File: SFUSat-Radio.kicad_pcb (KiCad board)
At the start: 4 copper layers, 95.9 x 90.2 mm, 283 parts, among them J1 PC104-8BIT, J10 TP_TH_150, J11 TP_TH_150, J12 SMA, J13 SMA, J14 SMA, J15 Conn_01x02, J16 SMA, J17 SMA, J18 SMA, J19 Conn_01x03, J2 PC104PTH, J20 Conn_01x03, J21 TP_TH_150, J22 TP_TH_150, J23 TP_TH_150, J24 TP_TH_150, J25 Conn_01x02, J3 PC104PTH, J4 PC104PTH, J400 SMA, J401 TP_TH_150, J402 TP_TH_150, J404 TP_TH_150, J405 TP_TH_150, J406 TP_TH_150, J5 PC104PTH, J500 SMA, J501 TP_TH_150, J502 TP_TH_150, J504 TP_TH_150, J505 TP_TH_150, J506 TP_TH_150, J6 SMA, J7 TP_TH_150, J8 TP_TH_150, J9 TP_TH_150, U1 SINGLE_0402, U10 TPS799, U100 CC1101-Q1, U101 0433BM15A0001, U11 SINGLE_0402, U110 CC1101-Q1, U111 0915BM15A0001E, U12 CONN_02X05_SHRD, U13 CONN_02X05_SHRD, U14 2N7002DW, U15 TPS62175DQCR, U16 TPS71750DSER, U17 74LVC1G14SE-7, U2 SKY13345-368LF, U3 CD4555BPWR, U4 LMS3635AQRNLRQ1, U400 SINGLE_0402, U401 LMV358, U402 RF6886, U420 2N7002DW, U5 MML09211H, U500 SINGLE_0402, U501 LMV358, U502 RF6886, U6 SINGLE_0402, U600 STLM75, U610 STLM75, U7 SKY13372-467LF, U8 SINGLE_0402, U9 TLV702, X100 NX3225GA, X110 NX3225GA

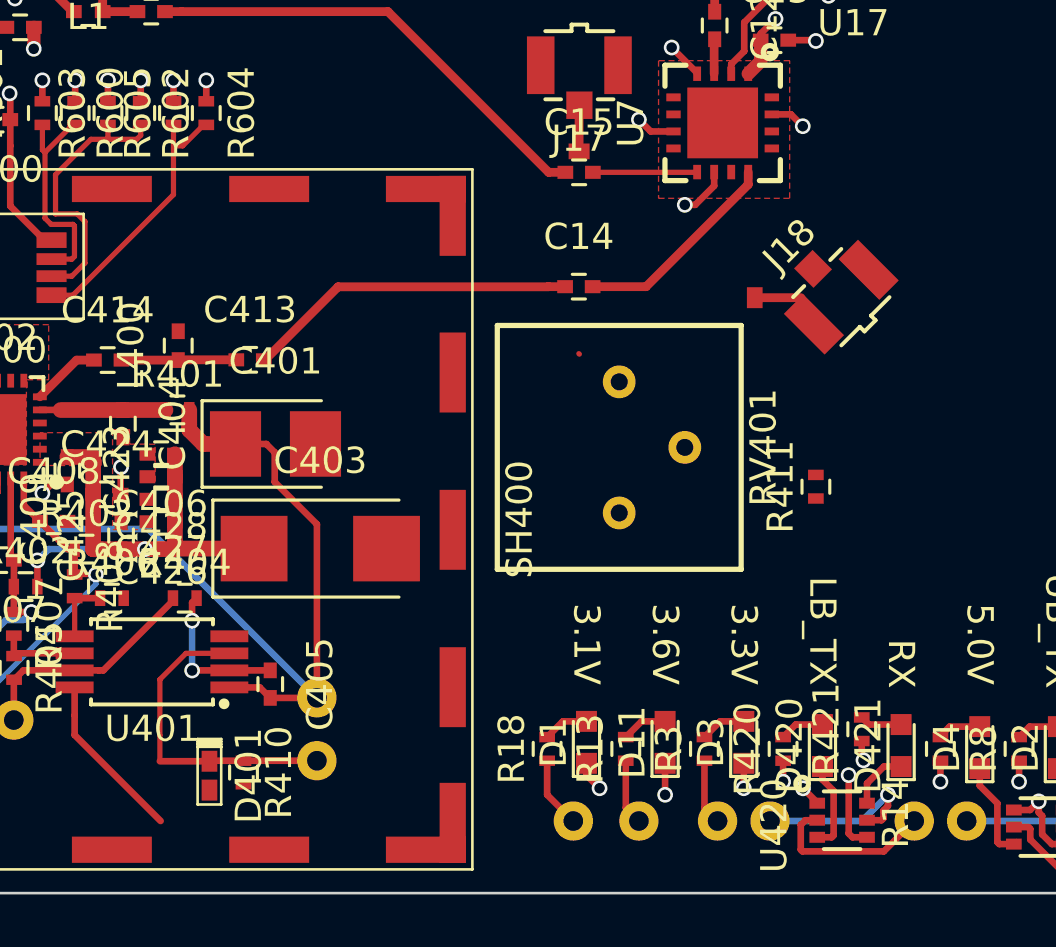
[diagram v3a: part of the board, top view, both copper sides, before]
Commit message: fixed LB cc1101 test point
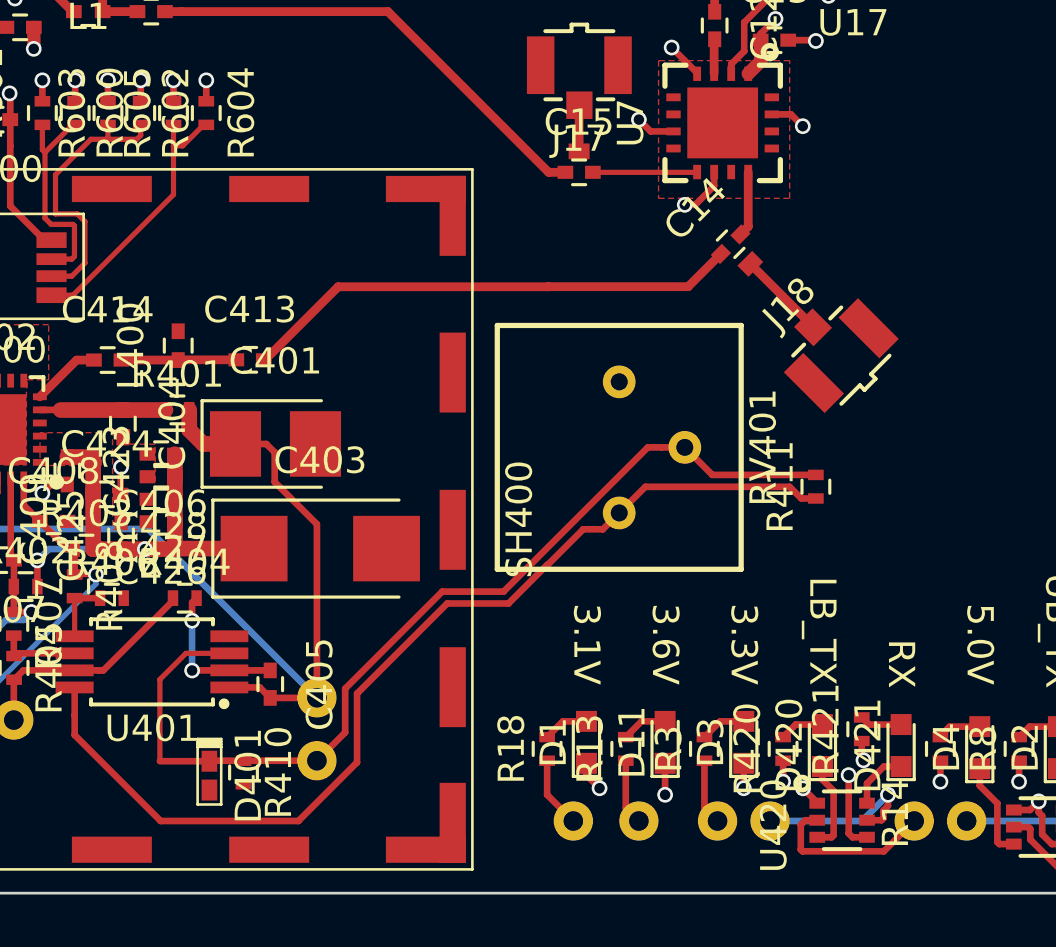
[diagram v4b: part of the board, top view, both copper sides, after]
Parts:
- moved C14 6.01 mm to (180.8, 123.8), turned to 45 degrees
- moved J18 2.23 mm to (185.0, 128.0)
- moved U8 1.30 mm to (181.5, 124.5), turned to 225 degrees
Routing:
- net /3V1: track 96.1 -> 128.1 mm
- net /PA_LB/GAIN: track 12.2 -> 37.6 mm
- net /LB_LP_TX: track 12.6 -> 19.1 mm
- net Net-(C14-Pad2): track 8.02 -> 2.50 mm
- net Net-(J18-Pad1): track 1.78 -> 3.41 mm

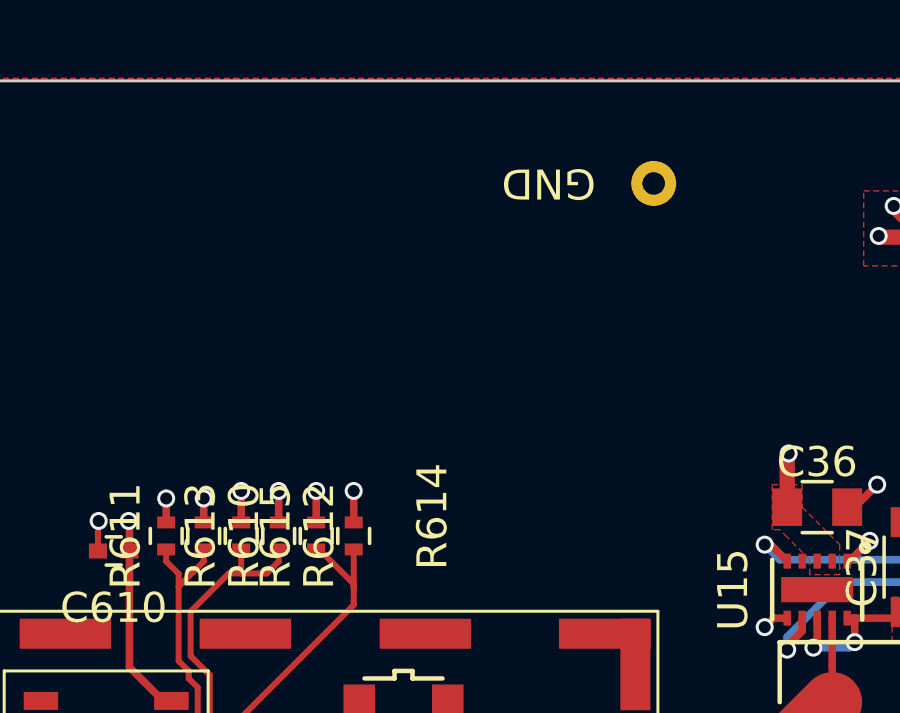
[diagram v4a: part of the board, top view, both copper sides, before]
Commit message: Added barrel jack for Vin; closes 46
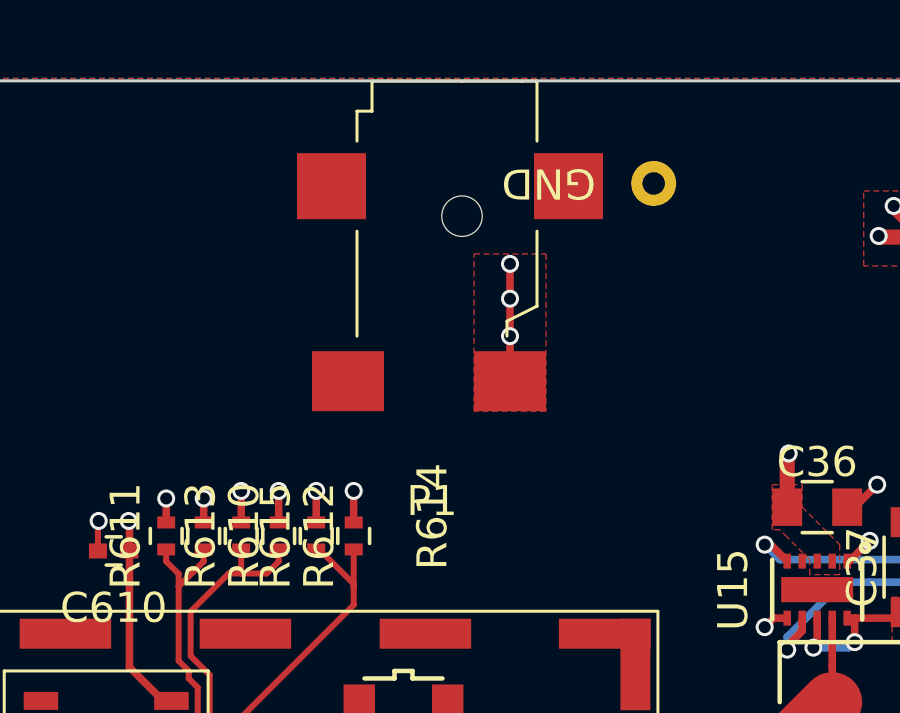
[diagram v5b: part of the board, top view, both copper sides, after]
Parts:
- added P1: 3pin-DC-power, SFUSat:PJ-028-SMT-TR-3pin-DC-jack, F.Cu at (146.4, 62.8)
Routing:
- net /VIN: track 12.4 -> 16.3 mm, vias 4 -> 7
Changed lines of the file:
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@@
-(kicad_pcb (version 4) (host pcbnew 4.0.7-e2-6376~58~ubuntu16.04.1)
+(kicad_pcb (version 4) (host pcbnew 4.0.5)
   (general
-    (links 728)
-    (no_connects 103)
+    (links 732)
+    (no_connects 78)
     (area 112.449999 58.279999 208.440001 148.550001)
     (thickness 1.6)
     (drawings 26)
-    (tracks 1228)
+    (tracks 1234)
     (zones 0)
-    (modules 283)
+    (modules 284)
     (nets 207)
   )
@@
     )
   )
+  (module SFUSat:PJ-028-SMT-TR-3pin-DC-jack (layer F.Cu)
+    (at 146.36 62.84 270)
+    (fp_text reference P1 (at 9.5 1 360) (layer F.SilkS)
+      (effects (font (size 1 1) (thickness 0.15)))
+    )
+    (fp_text value 3pin-DC-power (at 3.5 -6.5 270) (layer F.Fab)
+      (effects (font (size 1 1) (thickness 0.15)))
+    )
+    (fp_line (start 3.5 -1.5) (end 4 -1.5) (layer F.SilkS) (width 0.1))
+    (fp_line (start 3 -2.5) (end 3.5 -1.5) (layer F.SilkS) (width 0.1))
+    (fp_line (start 0.5 -2.5) (end 3 -2.5) (layer F.SilkS) (width 0.1))
+    (fp_line (start 0.5 3.5) (end 4 3.5) (layer F.SilkS) (width 0.1))
+    (fp_line (start -4.5 -2.5) (end -2.5 -2.5) (layer F.SilkS) (width 0.1))
+    (fp_line (start -4.5 -2) (end -4.5 -2.5) (layer F.SilkS) (width 0.1))
+    (fp_line (start -4.5 3) (end -4.5 0) (layer F.SilkS) (width 0.1))
+    (fp_line (start -3.5 3) (end -4.5 3) (layer F.SilkS) (width 0.1))
+    (fp_line (start -3.5 3.5) (end -3.5 3) (layer F.SilkS) (width 0.1))
+    (fp_line (start -2.5 3.5) (end -3.5 3.5) (layer F.SilkS) (width 0.1))
+    (fp_line (start -4.5 0) (end -4.5 -2) (layer F.SilkS) (width 0.1))
+    (pad 3 smd rect (at -1 -3.55 270) (size 2.2 2.3) (layers F.Cu F.Paste F.Mask)
+      (net 1 GND))
+    (pad "" np_thru_hole circle (at 0 0 270) (size 1.35 1.35) (drill 1.35) (layers *.Cu *.Mask))
+    (pad 3 smd rect (at -1 4.35 270) (size 2.2 2.3) (layers F.Cu F.Paste F.Mask)
+      (net 1 GND))
+    (pad 2 smd rect (at 5.5 3.8 270) (size 2 2.4) (layers F.Cu F.Paste F.Mask)
+      (net 1 GND))
+    (pad 1 smd rect (at 5.5 -1.6 270) (size 2 2.4) (layers F.Cu F.Paste F.Mask)
+      (net 183 /VIN))
+  )
   (gr_text GND (at 149.25 61.75 180) (layer F.SilkS)
     (effects (font (size 1 1) (thickness 0.15)))
@@
   (segment (start 182.42 96.13) (end 182.82 95.73) (width 0.2) (layer F.Cu) (net 170))
   (segment (start 182.82 95.73) (end 184.095 95.73) (width 0.2) (layer F.Cu) (net 170))
+  (segment (start 147.96 65.59) (end 147.96 64.43) (width 0.254) (layer F.Cu) (net 183))
+  (via (at 147.96 64.43) (size 0.6) (drill 0.4) (layers F.Cu B.Cu) (net 183))
+  (segment (start 147.96 66.84) (end 147.96 65.59) (width 0.254) (layer F.Cu) (net 183))
+  (via (at 147.96 65.59) (size 0.6) (drill 0.4) (layers F.Cu B.Cu) (net 183))
+  (segment (start 147.96 68.34) (end 147.96 66.84) (width 0.254) (layer F.Cu) (net 183))
+  (via (at 147.96 66.84) (size 0.6) (drill 0.4) (layers F.Cu B.Cu) (net 183))
   (segment (start 163.8 63.54) (end 160.29 63.54) (width 0.508) (layer F.Cu) (net 183))
   (segment (start 160.29 63.54) (end 160.25 63.5) (width 0.508) (layer F.Cu) (net 183))
@@
       (pts
         (xy 192.75 69.25) (xy 169.5 69.25) (xy 169.5 69.75) (xy 169.5 84.25) (xy 155.75 84.25)
-        (xy 155.75 58.25) (xy 192.5 58.25) (xy 192.75 58.25)
+        (xy 155.76 69.33) (xy 146.76 69.34) (xy 146.76 58.25) (xy 192.5 58.25) (xy 192.75 58.25)
       )
     )
@@
       )
     )
+  )
+  (zone (net 183) (net_name /VIN) (layer F.Cu) (hatch edge 0.508)
+    (priority 1)
+    (connect_pads yes (clearance 0.154))
+    (min_thickness 0.254)
+    (fill yes (arc_segments 16) (thermal_gap 0.508) (thermal_bridge_width 0.508))
+    (polygon
+      (pts
+        (xy 146.76 64.1) (xy 149.16 64.1) (xy 149.16 69.34) (xy 146.76 69.34)
+      )
+    )

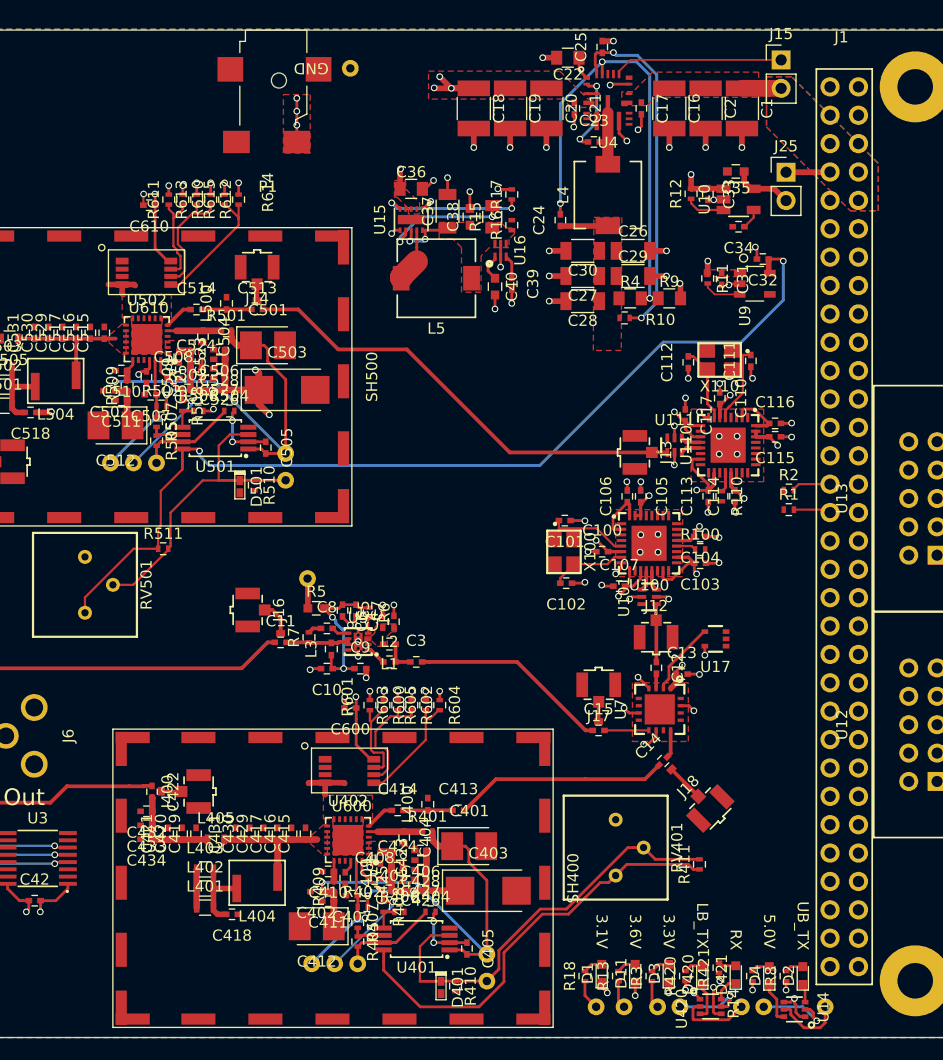
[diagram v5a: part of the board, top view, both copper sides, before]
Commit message: Continued power floods
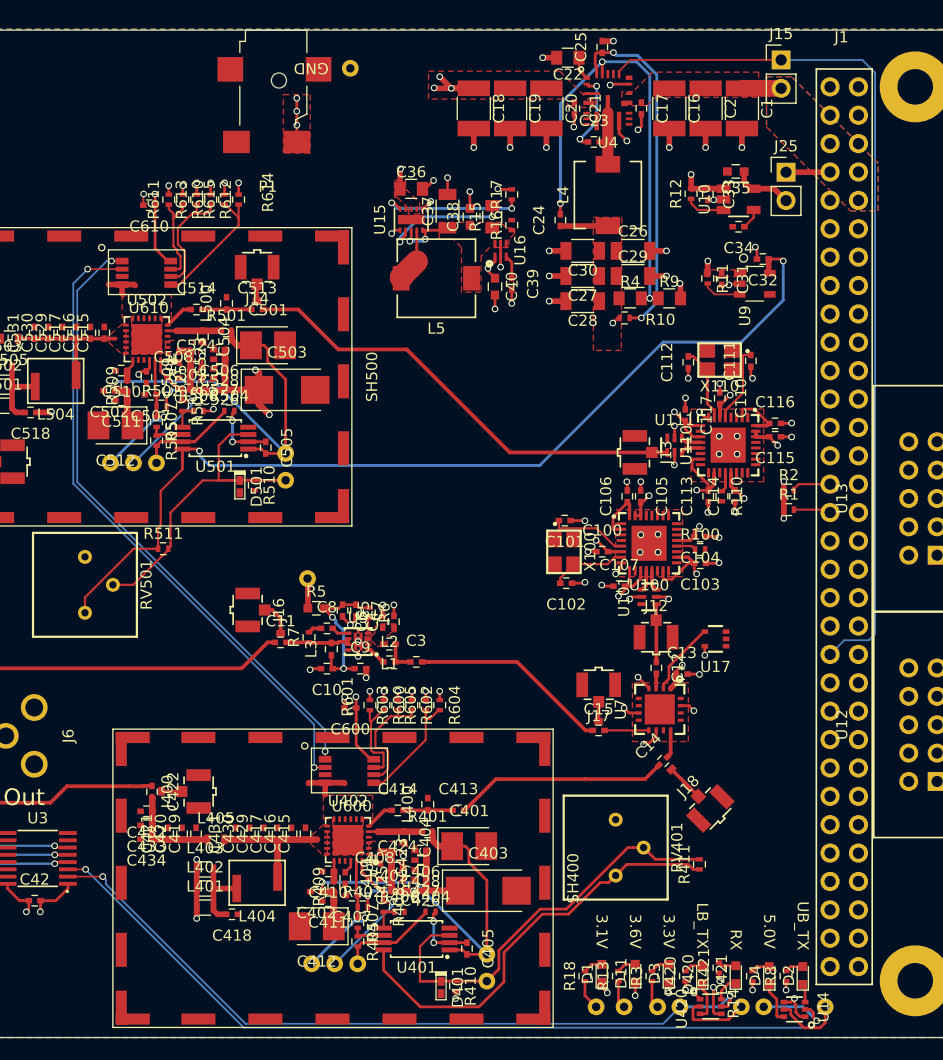
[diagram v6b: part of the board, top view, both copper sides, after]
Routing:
- net /UB_RX0TX1: track 6.23 -> 81.5 mm, vias 0 -> 1
- net /EN_3V6: track 15.2 -> 79.1 mm
- net /LB_RX0TX1: track 6.58 -> 67.7 mm, vias 1 -> 2
- net /SCL: track 3.52 -> 61.7 mm, vias 0 -> 2
- net /SDA: track 3.35 -> 59.6 mm, vias 0 -> 2
- net /3V6: track 68.4 -> 105.2 mm, vias 11 -> 14
- net /3V3: track 38.0 -> 41.3 mm, vias 16 -> 18
- net GND: track 119.7 -> 120.4 mm, vias 95 -> 96
- net /5V0: vias 1 -> 2
